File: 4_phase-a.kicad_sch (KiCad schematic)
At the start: 28 parts, among them Q401 BSC072N08NS5, Q402 BSC072N08NS5, U401 IR2181S, U402 AD8418

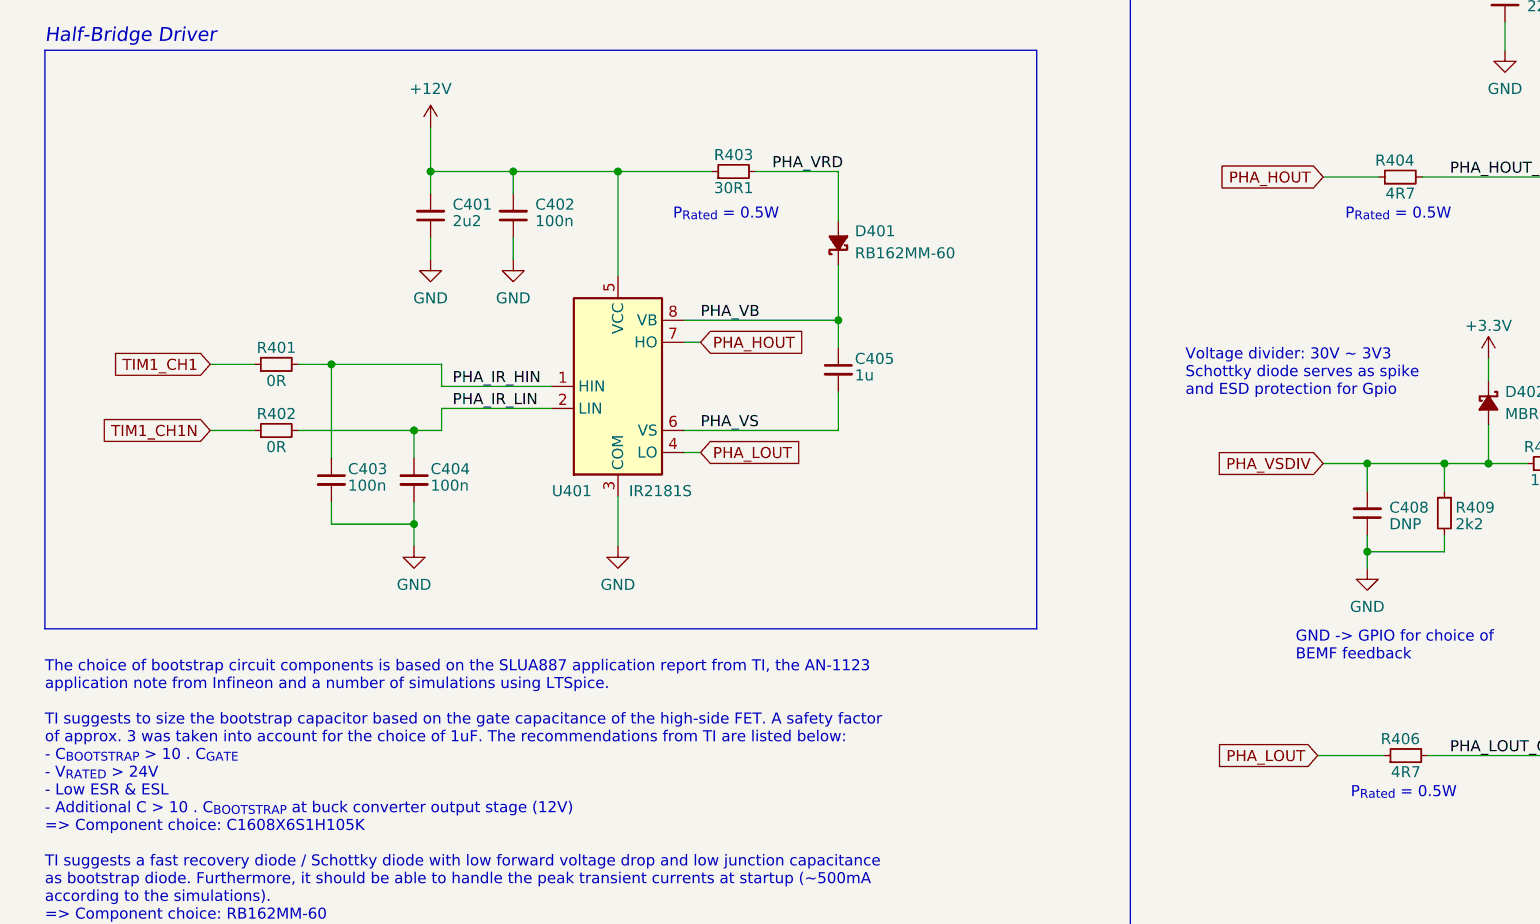
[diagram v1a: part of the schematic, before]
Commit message: global labels to local labels wherever possible and mcu pinout addition
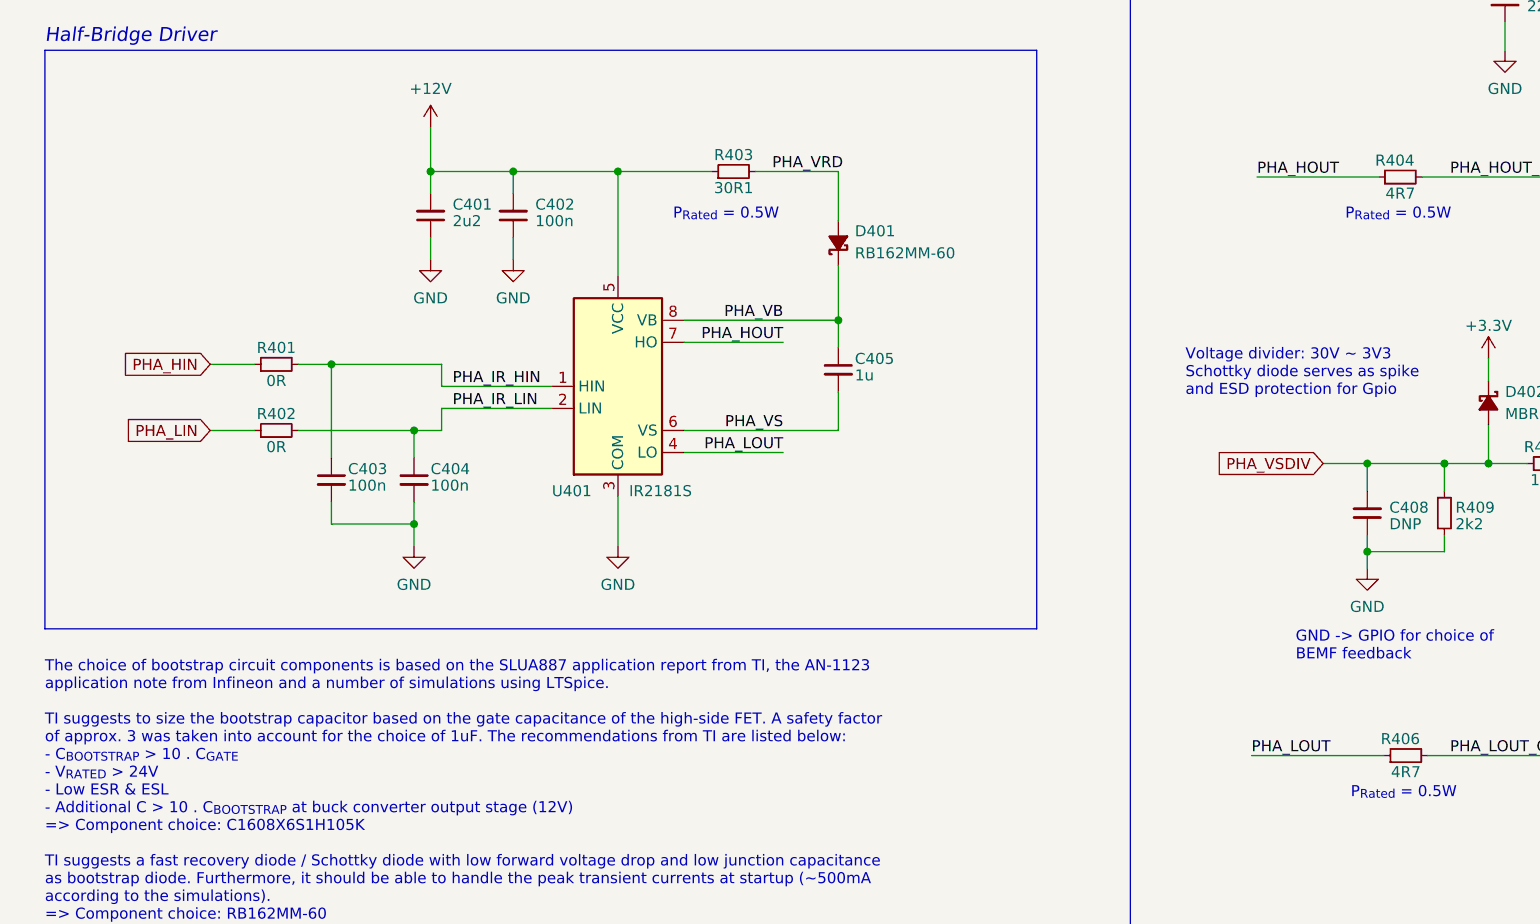
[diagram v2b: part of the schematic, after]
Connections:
- net TIM1_CH1 renamed PHA_HIN
- net TIM1_CH1N renamed PHA_LIN
